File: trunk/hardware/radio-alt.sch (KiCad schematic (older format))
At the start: 19 parts, among them U3 AT86RF231, Y1 NX3225SA-16MHz-15ppm

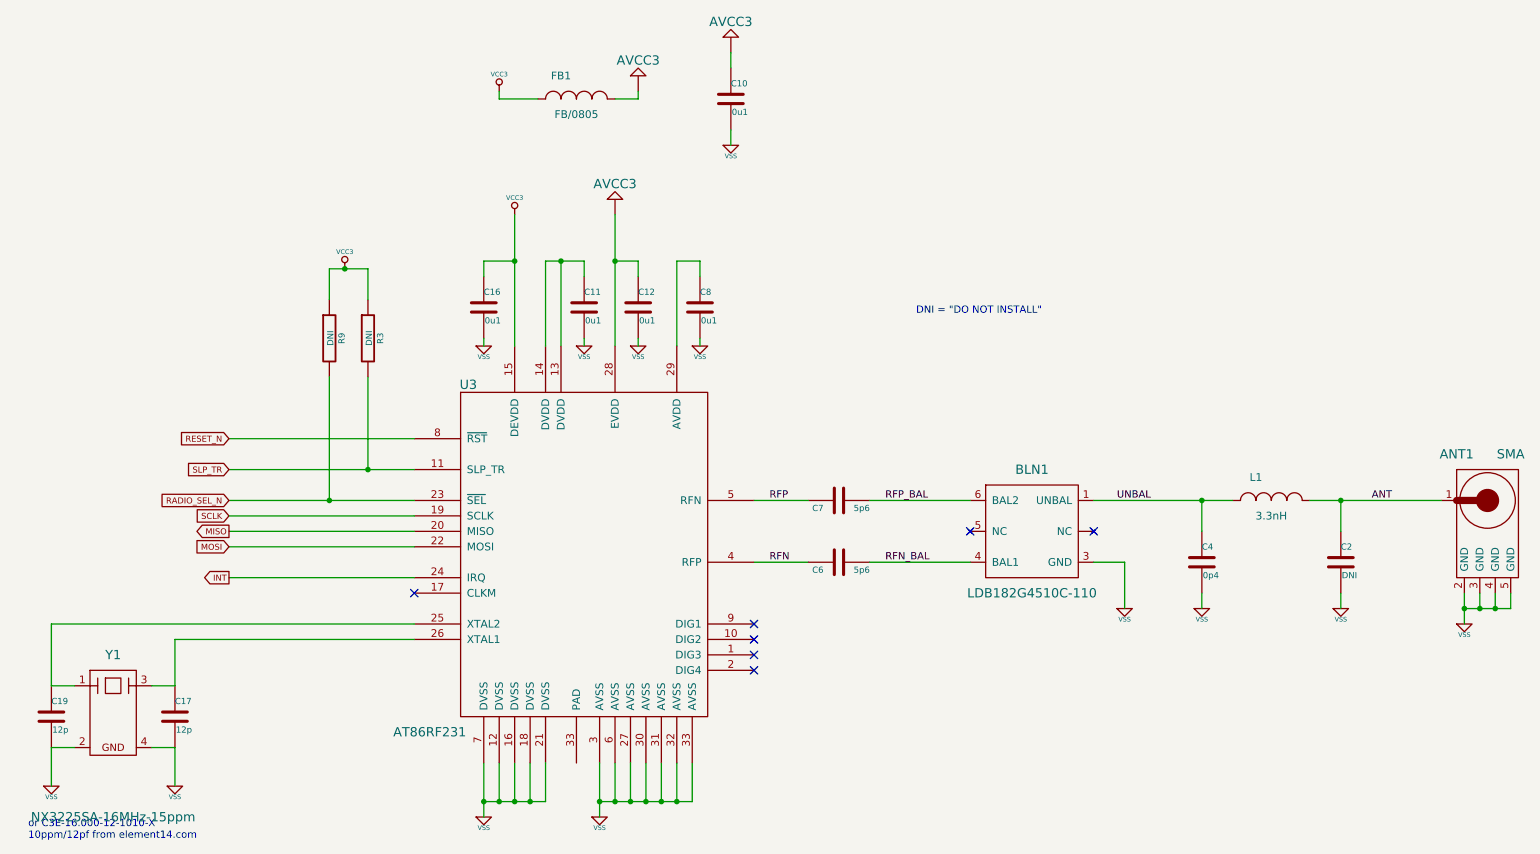
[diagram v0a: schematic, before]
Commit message: CHANGING to -ALT files form this point onwards ...
Due to a number of changes from the original Freakduino design, I'm now
continuing my design in the freakduino-alt project, leaving a copy of the 
original work in the files without -alt.

The single shre/ folder (freakduino.lib, etc) will contain components,
and 3D modules for both versions.
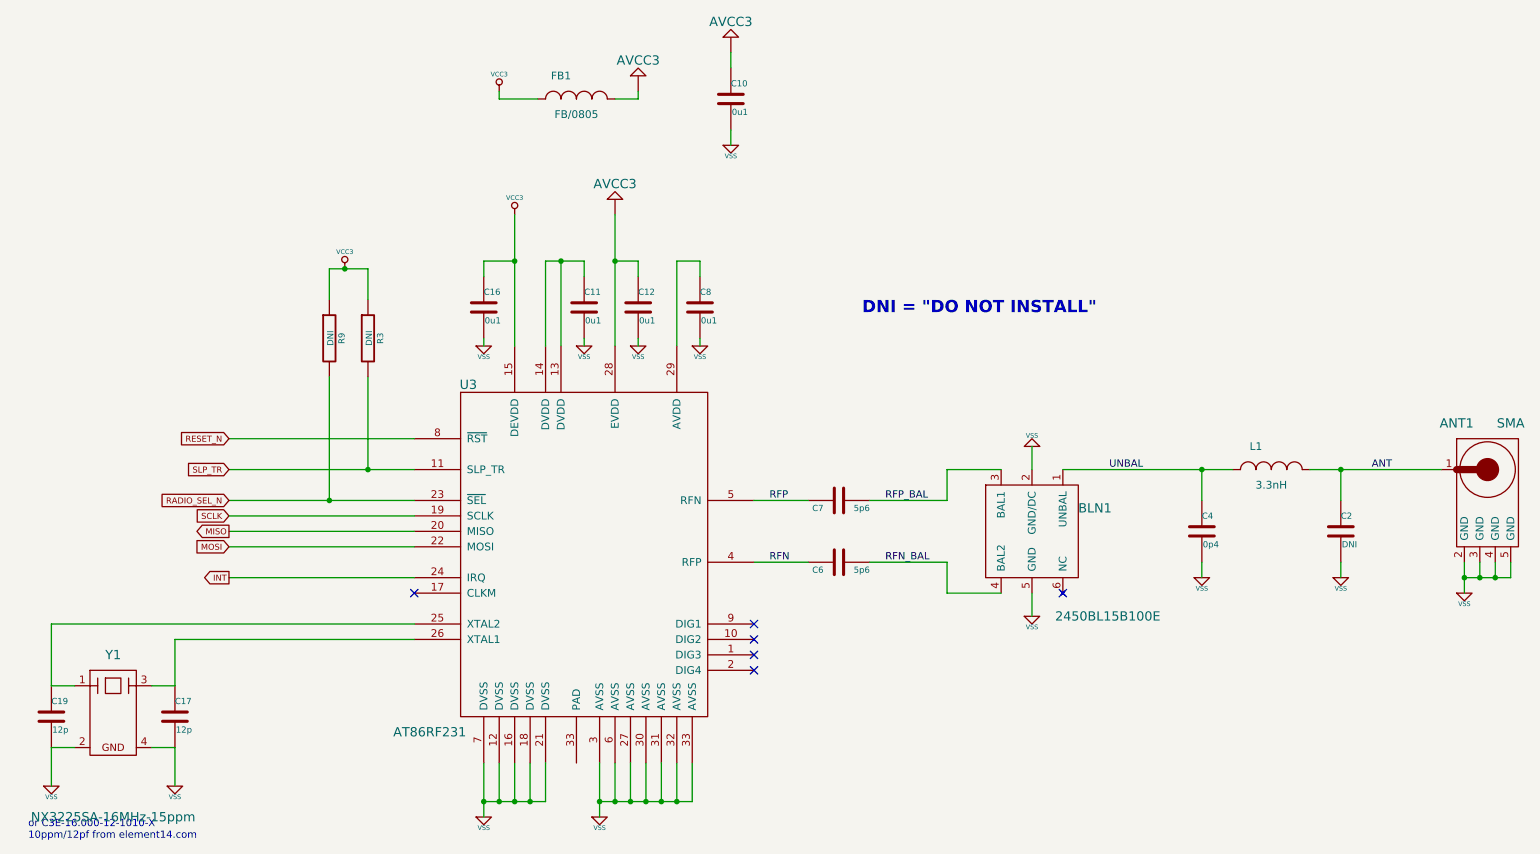
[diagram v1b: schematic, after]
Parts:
- removed BLN1: LDB182G4510C-110, symbol LDB182G4510C-110
- added BLN1: 2450BL15B100E, ~, symbol BALUN_GRUVIN
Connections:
- net RFN_BAL: now also BLN1.4 (BAL2)
- net RFP_BAL: now also BLN1.3 (BAL1)
- net UNBAL: now also BLN1.1 (UNBAL)
- net VSS: now also BLN1.2 (GND/DC), BLN1.5 (GND)
- no-connect marks 7 -> 6
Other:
- moved on the sheet: ANT1, C2, C4, L1
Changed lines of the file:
@@
 $Descr A4 11693 8268
 encoding utf-8
-Sheet 3 6
+Sheet 2 6
 Title "FREAKDUINO-CHIBI 2.4GHz"
 Date "18 jul 2013"
@@
 	4700 2150 4700 3000
 Wire Wire Line
-	4050 3000 4050 2150
+	4050 2150 4050 3000
 $Comp
 L VCC3 #PWR014
@@
 Wire Wire Line
 	5950 4400 5600 4400
-$Comp
-L LDB182G4510C-110 BLN1
-U 1 1 51E3A326
-P 7400 4200
-F 0 "BLN1" H 7400 4600 60  0000 C CNN
-F 1 "LDB182G4510C-110" H 7400 3800 60  0000 C CNN
-F 2 "" H 7400 4200 60  0000 C CNN
-F 3 "" H 7400 4200 60  0000 C CNN
-	1    7400 4200
-	1    0    0    -1
-$EndComp
-Wire Wire Line
-	6350 4000 7000 4000
-Wire Wire Line
-	7000 4400 6350 4400
-NoConn ~ 7800 4200
-NoConn ~ 7000 4200
+Wire Wire Line
+	6350 4000 6850 4000
+Wire Wire Line
+	6850 4400 6350 4400
 Text Label 6450 4000 0    47   ~ 0
 RFP_BAL
@@
 L INDUCTOR_SMALL L1
 U 1 1 51E3A3E1
-P 8950 4000
-F 0 "L1" H 8850 4150 50  0000 C CNN
-F 1 "3.3nH" H 8950 3900 50  0000 C CNN
-F 2 "" H 8950 4000 60  0000 C CNN
-F 3 "" H 8950 4000 60  0000 C CNN
-	1    8950 4000
+P 8950 3800
+F 0 "L1" H 8850 3950 50  0000 C CNN
+F 1 "3.3nH" H 8950 3700 50  0000 C CNN
+F 2 "" H 8950 3800 60  0000 C CNN
+F 3 "" H 8950 3800 60  0000 C CNN
+	1    8950 3800
 	1    0    0    -1
 $EndComp
@@
 L C C4
 U 1 1 51E3A3F1
-P 8500 4400
-F 0 "C4" H 8500 4500 40  0000 L CNN
-F 1 "0p4" H 8506 4315 40  0000 L CNN
-F 2 "" H 8538 4250 30  0000 C CNN
-F 3 "" H 8500 4400 60  0000 C CNN
-	1    8500 4400
+P 8500 4200
+F 0 "C4" H 8500 4300 40  0000 L CNN
+F 1 "0p4" H 8506 4115 40  0000 L CNN
+F 2 "" H 8538 4050 30  0000 C CNN
+F 3 "" H 8500 4200 60  0000 C CNN
+	1    8500 4200
 	1    0    0    -1
 $EndComp
@@
 L C C2
 U 1 1 51E3A3F7
-P 9400 4400
-F 0 "C2" H 9400 4500 40  0000 L CNN
-F 1 "DNI" H 9406 4315 40  0000 L CNN
-F 2 "" H 9438 4250 30  0000 C CNN
-F 3 "" H 9400 4400 60  0000 C CNN
-	1    9400 4400
-	1    0    0    -1
-$EndComp
-Wire Wire Line
-	8700 4000 7800 4000
-Wire Wire Line
-	8500 4200 8500 4000
-Connection ~ 8500 4000
-Wire Wire Line
-	9200 4000 10050 4000
-Wire Wire Line
-	9400 4200 9400 4000
-Connection ~ 9400 4000
-Text Label 7950 4000 0    47   ~ 0
+P 9400 4200
+F 0 "C2" H 9400 4300 40  0000 L CNN
+F 1 "DNI" H 9406 4115 40  0000 L CNN
+F 2 "" H 9438 4050 30  0000 C CNN
+F 3 "" H 9400 4200 60  0000 C CNN
+	1    9400 4200
+	1    0    0    -1
+$EndComp
+Wire Wire Line
+	7600 3800 8700 3800
+Wire Wire Line
+	8500 4000 8500 3800
+Connection ~ 8500 3800
+Wire Wire Line
+	9200 3800 10050 3800
+Wire Wire Line
+	9400 4000 9400 3800
+Connection ~ 9400 3800
+Text Label 7900 3800 0    47   ~ 0
 UNBAL
-Text Label 9600 4000 0    47   ~ 0
+Text Label 9600 3800 0    47   ~ 0
 ANT
 $Comp
 L VSS #PWR025
 U 1 1 51E3A542
-P 8500 4700
-F 0 "#PWR025" H 8500 4700 30  0001 C CNN
-F 1 "VSS" H 8500 4630 30  0000 C CNN
-F 2 "" H 8500 4700 60  0000 C CNN
-F 3 "" H 8500 4700 60  0000 C CNN
-	1    8500 4700
+P 8500 4500
+F 0 "#PWR025" H 8500 4500 30  0001 C CNN
+F 1 "VSS" H 8500 4430 30  0000 C CNN
+F 2 "" H 8500 4500 60  0000 C CNN
+F 3 "" H 8500 4500 60  0000 C CNN
+	1    8500 4500
 	1    0    0    -1
 $EndComp
@@
 L VSS #PWR026
 U 1 1 51E3A548
-P 9400 4700
-F 0 "#PWR026" H 9400 4700 30  0001 C CNN
-F 1 "VSS" H 9400 4630 30  0000 C CNN
-F 2 "" H 9400 4700 60  0000 C CNN
-F 3 "" H 9400 4700 60  0000 C CNN
-	1    9400 4700
-	1    0    0    -1
-$EndComp
-Wire Wire Line
-	8500 4700 8500 4600
-Wire Wire Line
-	9400 4600 9400 4700
+P 9400 4500
+F 0 "#PWR026" H 9400 4500 30  0001 C CNN
+F 1 "VSS" H 9400 4430 30  0000 C CNN
+F 2 "" H 9400 4500 60  0000 C CNN
+F 3 "" H 9400 4500 60  0000 C CNN
+	1    9400 4500
+	1    0    0    -1
+$EndComp
+Wire Wire Line
+	8500 4500 8500 4400
+Wire Wire Line
+	9400 4400 9400 4500
 $Comp
 L VSS #PWR027
 U 1 1 51E3A80A
-P 8000 4700
-F 0 "#PWR027" H 8000 4700 30  0001 C CNN
-F 1 "VSS" H 8000 4630 30  0000 C CNN
-F 2 "" H 8000 4700 60  0000 C CNN
-F 3 "" H 8000 4700 60  0000 C CNN
-	1    8000 4700
-	1    0    0    -1
-$EndComp
-Wire Wire Line
-	7800 4400 8000 4400
-Wire Wire Line
-	8000 4400 8000 4700
+P 7400 4750
+F 0 "#PWR027" H 7400 4750 30  0001 C CNN
+F 1 "VSS" H 7400 4680 30  0000 C CNN
+F 2 "" H 7400 4750 60  0000 C CNN
+F 3 "" H 7400 4750 60  0000 C CNN
+	1    7400 4750
+	1    0    0    -1
+$EndComp
+Wire Wire Line
+	7400 4600 7400 4750
 Text Label 5700 4000 0    47   ~ 0
 RFP
 Text Label 5700 4400 0    47   ~ 0
 RFN
-Text Notes 6650 2800 0    47   ~ 0
-DNI = "DO NOT INSTALL"
 $Comp
 L SMA ANT1
 U 1 1 51E3A9AC
-P 10350 4250
-F 0 "ANT1" H 10150 4800 60  0000 C CNN
-F 1 "SMA" H 10500 4800 60  0000 C CNN
-F 2 "" H 10350 4250 60  0000 C CNN
-F 3 "" H 10350 4250 60  0000 C CNN
-	1    10350 4250
+P 10350 4050
+F 0 "ANT1" H 10150 4600 60  0000 C CNN
+F 1 "SMA" H 10500 4600 60  0000 C CNN
+F 2 "" H 10350 4050 60  0000 C CNN
+F 3 "" H 10350 4050 60  0000 C CNN
+	1    10350 4050
 	1    0    0    -1
 $EndComp
@@
 L VSS #PWR028
 U 1 1 51E3A9B9
-P 10200 4800
-F 0 "#PWR028" H 10200 4800 30  0001 C CNN
-F 1 "VSS" H 10200 4730 30  0000 C CNN
-F 2 "" H 10200 4800 60  0000 C CNN
-F 3 "" H 10200 4800 60  0000 C CNN
-	1    10200 4800
-	1    0    0    -1
-$EndComp
-Wire Wire Line
-	10200 4600 10200 4800
-Wire Wire Line
-	10300 4600 10300 4700
-Wire Wire Line
-	10200 4700 10500 4700
-Connection ~ 10200 4700
-Wire Wire Line
-	10400 4700 10400 4600
-Connection ~ 10300 4700
-Wire Wire Line
-	10500 4700 10500 4600
-Connection ~ 10400 4700
+P 10200 4600
+F 0 "#PWR028" H 10200 4600 30  0001 C CNN
+F 1 "VSS" H 10200 4530 30  0000 C CNN
+F 2 "" H 10200 4600 60  0000 C CNN
+F 3 "" H 10200 4600 60  0000 C CNN
+	1    10200 4600
+	1    0    0    -1
+$EndComp
+Wire Wire Line
+	10200 4400 10200 4600
+Wire Wire Line
+	10300 4400 10300 4500
+Wire Wire Line
+	10200 4500 10500 4500
+Connection ~ 10200 4500
+Wire Wire Line
+	10400 4500 10400 4400
+Connection ~ 10300 4500
+Wire Wire Line
+	10500 4500 10500 4400
+Connection ~ 10400 4500
 $Comp
 L C C16
@@
 Wire Wire Line
 	3850 3000 3850 2950
+$Comp
+L BALUN_GRUVIN BLN1
+U 1 1 51E793F4
+P 7400 4200
+F 0 "BLN1" H 7700 4350 60  0000 L CNN
+F 1 "2450BL15B100E" H 7550 3650 60  0000 L CNN
+F 2 "~" H 7400 4200 60  0000 C CNN
+F 3 "~" H 7400 4200 60  0000 C CNN
+	1    7400 4200
+	1    0    0    -1
+$EndComp
+Wire Wire Line
+	6850 4000 6850 3800
+Wire Wire Line
+	6850 3800 7200 3800
+Wire Wire Line
+	6850 4400 6850 4600
+Wire Wire Line
+	6850 4600 7200 4600
+$Comp
+L VSS #PWR030
+U 1 1 51E79531
+P 7400 3650
+F 0 "#PWR030" H 7400 3650 30  0001 C CNN
+F 1 "VSS" H 7400 3580 30  0000 C CNN
+F 2 "" H 7400 3650 60  0000 C CNN
+F 3 "" H 7400 3650 60  0000 C CNN
+	1    7400 3650
+	-1   0    0    1
+$EndComp
+Wire Wire Line
+	7400 3800 7400 3650
+NoConn ~ 7600 4600
+Text Notes 6300 2800 0    79   ~ 16
+DNI = "DO NOT INSTALL"
 $EndSCHEMATC

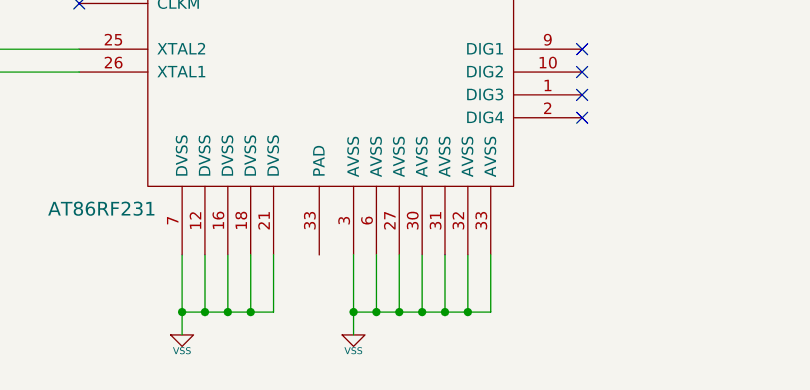
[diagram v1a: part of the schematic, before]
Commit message: Re-worked power supply boost circuit around an availabel part. Footprint and 3D package added for same.
Fixed multiple DRC errors with default KiCAD parts (saved in local 
library.)

Routed power boost circuit, paying attention to maximum GND/VSS 
shielding.

Set up fills for 50ohm (approx.) traces around radio chip and rest of 
board, both sides.

Updated BOM to reflect latest component changes.
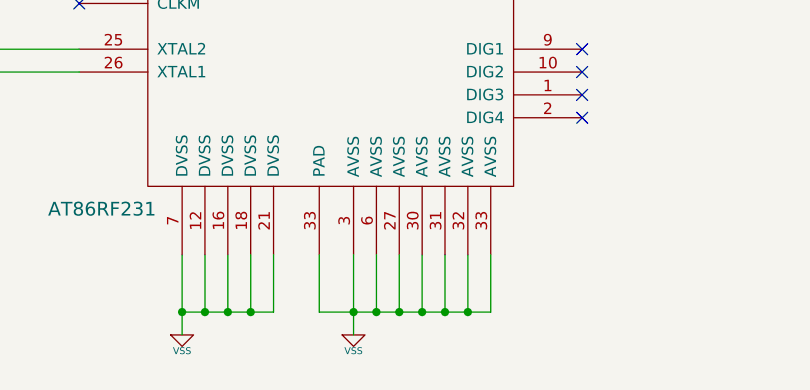
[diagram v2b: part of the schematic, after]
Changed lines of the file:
@@
 LIBS:contrib
 LIBS:valves
-LIBS:freakduino-cache
+LIBS:freakduino-alt-cache
 EELAYER 27 0
 EELAYER END
@@
 	4700 5700 4700 5950
 Wire Wire Line
-	4600 5950 5200 5950
+	4450 5950 5200 5950
 Connection ~ 4600 5950
 Wire Wire Line
@@
 Text Notes 6300 2800 0    79   ~ 16
 DNI = "DO NOT INSTALL"
+Wire Wire Line
+	4450 5700 4450 5950
 $EndSCHEMATC
